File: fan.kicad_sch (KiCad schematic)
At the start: 14 parts, among them J6 Conn_01x04, U10 EMC2101

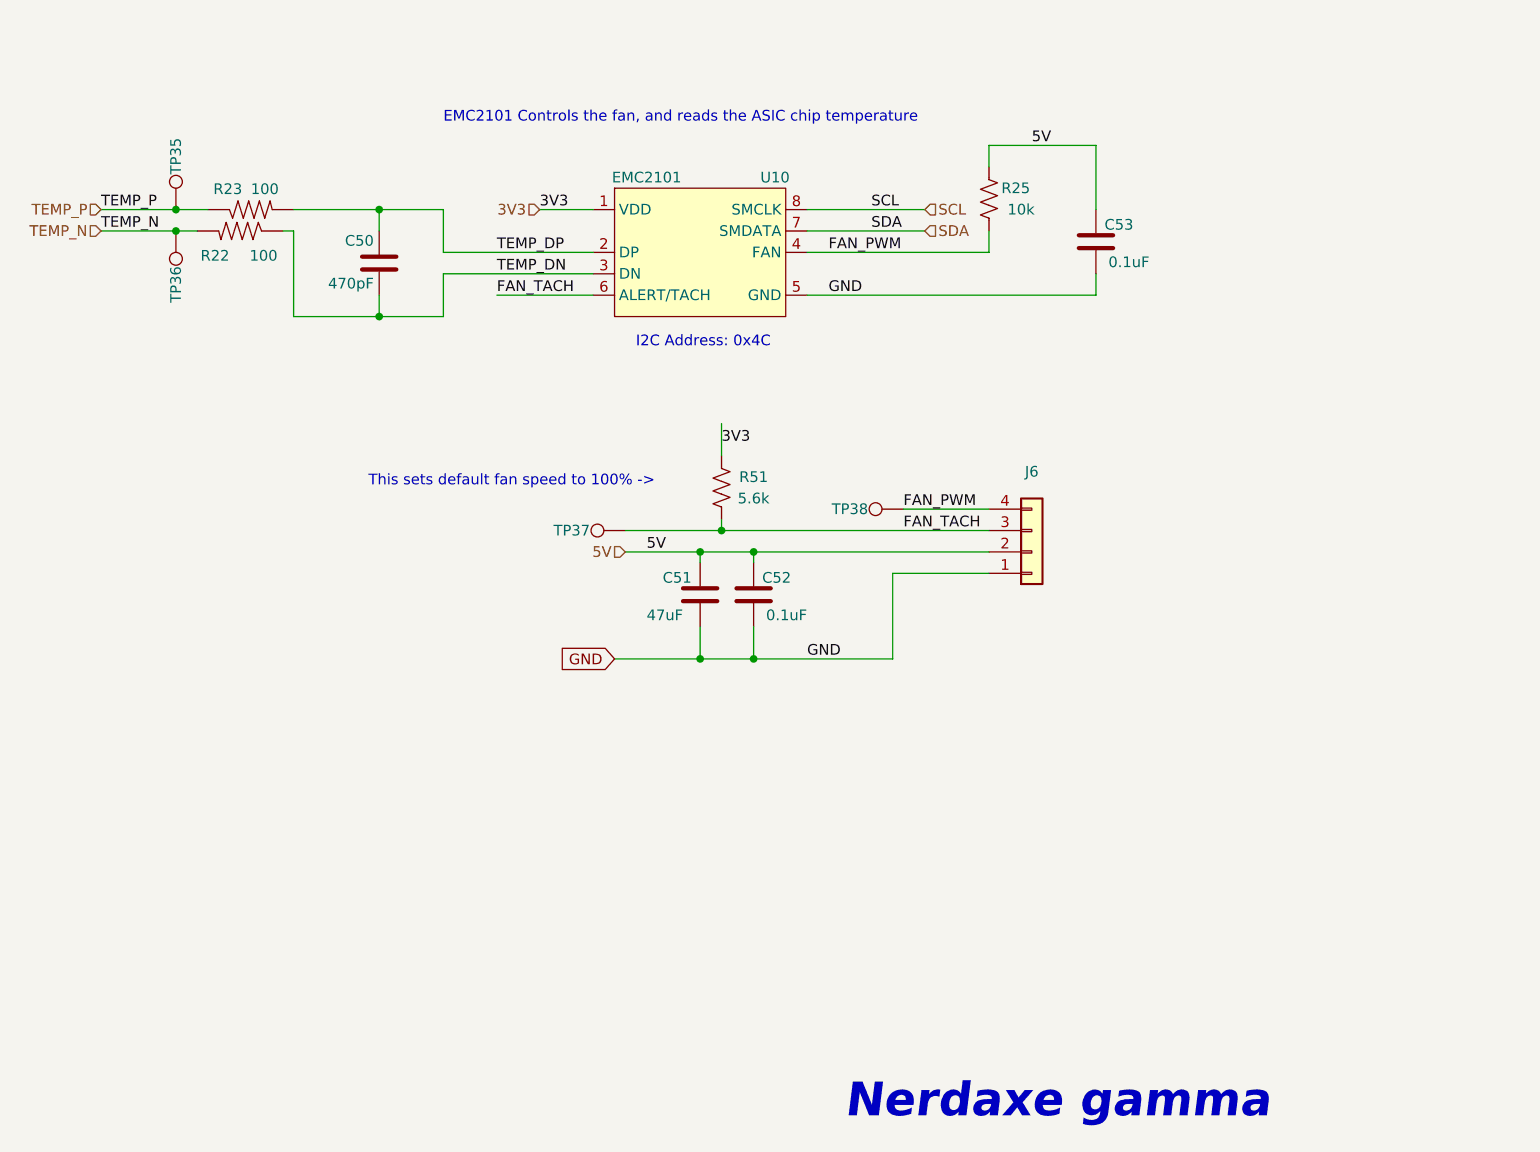
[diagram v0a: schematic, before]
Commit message: Nerdaxe Gamma v2.3
- Fix Emi CE needs
- Added ferrite beads + EMI blocking capacitors
- New components added: R16, R20, R26, R27C21, C22, C23, FB1, FB2, FB3, FB4, FB5, FB6
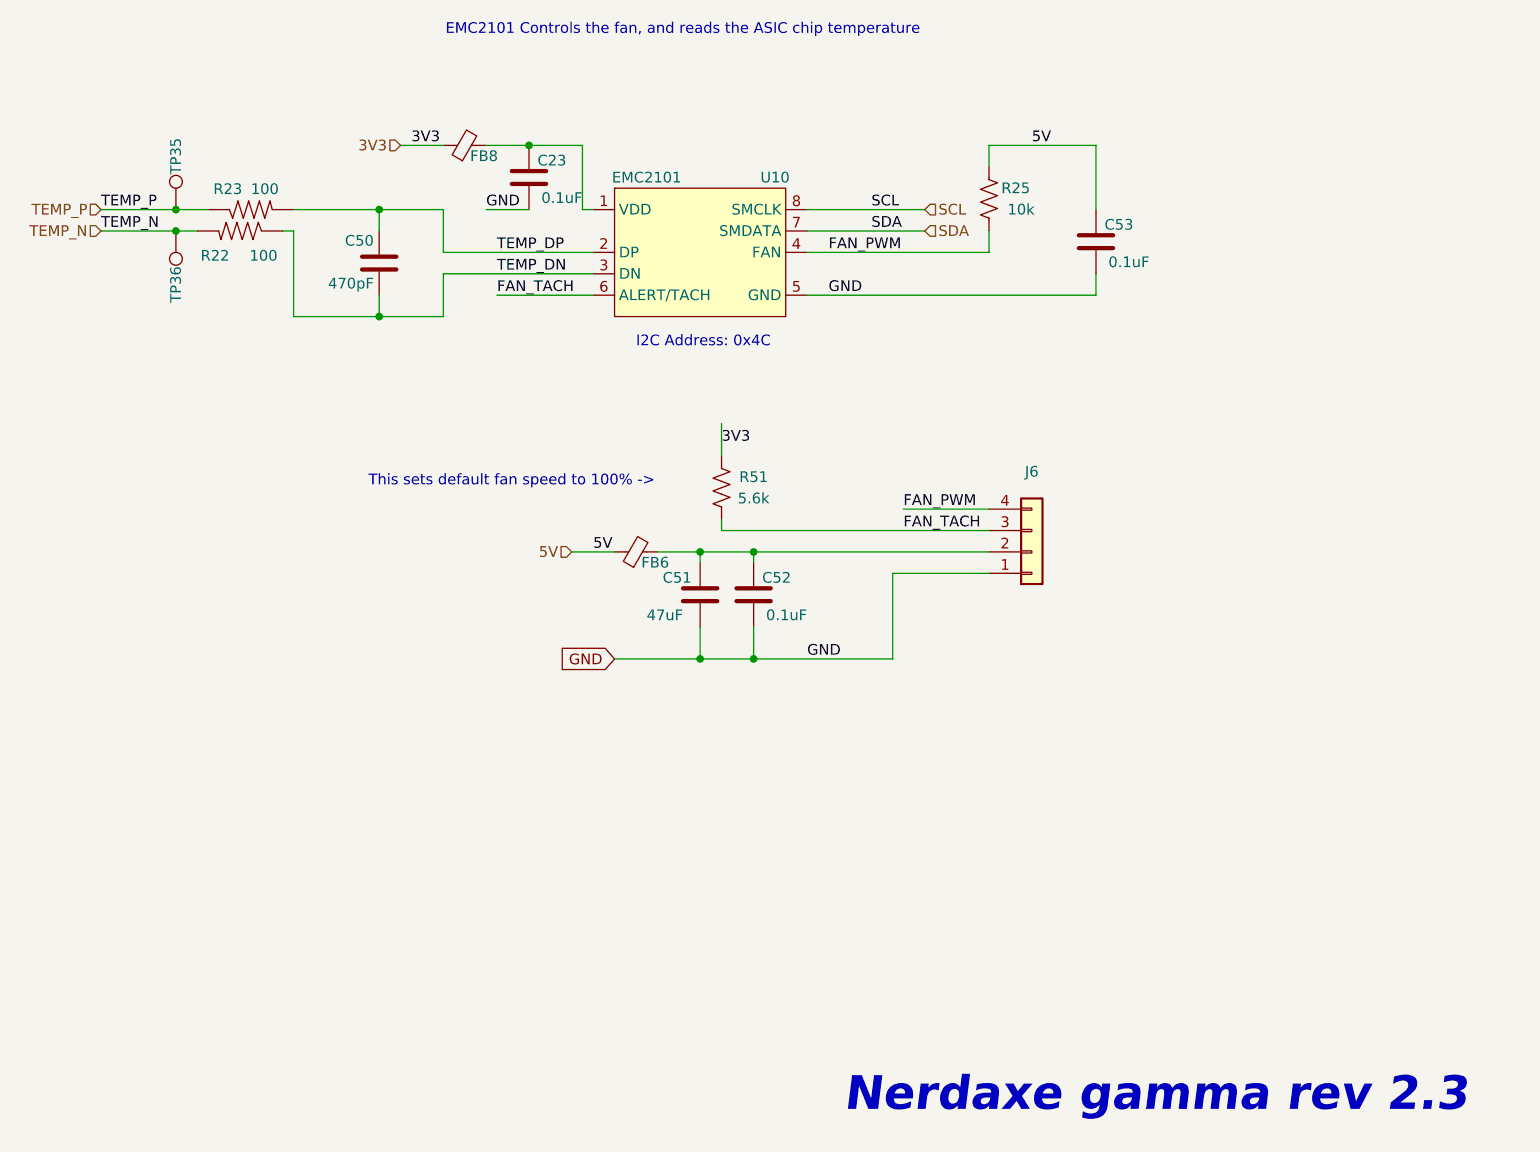
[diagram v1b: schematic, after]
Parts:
- removed TP37, TP38: TestPoint, TestPoint:TestPoint_Pad_D1.5mm, symbol Connector:TestPoint
- added C23: 0.1uF, Capacitor_SMD:C_0402_1005Metric, symbol Device:C
- added FB6, FB8: BLM21PG221SN1D, Resistor_SMD:R_0805_2012Metric, symbol Device:FerriteBead_Small
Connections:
- net 3V3: now also FB8.1; no longer U10.1 (VDD)
- net 5V: now also FB6.1; no longer C51.1, C52.1, J6.2 (Pin_2)
- net GND: now also C23.2
- new net: C51.1, C52.1, FB6.2, J6.2 (Pin_2)
- new net: C23.1, FB8.2, U10.1 (VDD)
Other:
- note added: "Nerdaxe gamma rev 2.3"
- note removed: "Nerdaxe gamma"
- title: bitaxeGamma -> NerdaxeGamma
